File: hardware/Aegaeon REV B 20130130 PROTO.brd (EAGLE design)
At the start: 9.2 x 15.2 mm, 39 parts, among them IC1 ATTINY84A-MMH, Q1 DMN65D8LDW, U1 V_REG_LDOSMD

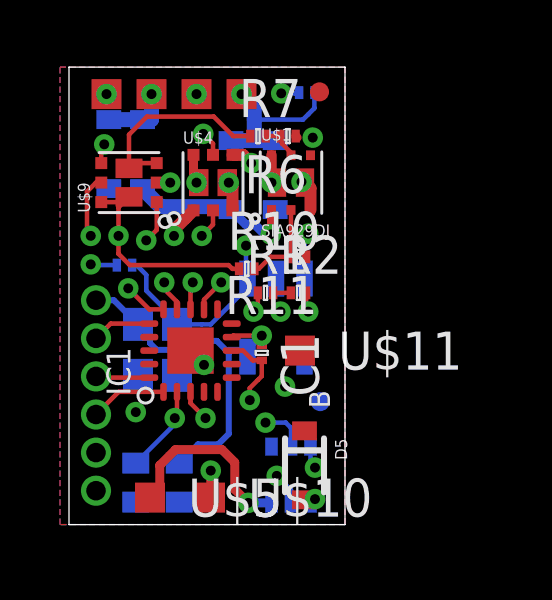
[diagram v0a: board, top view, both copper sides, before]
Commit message: Updated proto schematics to match new bridge design. Streamlined design in simulation file.
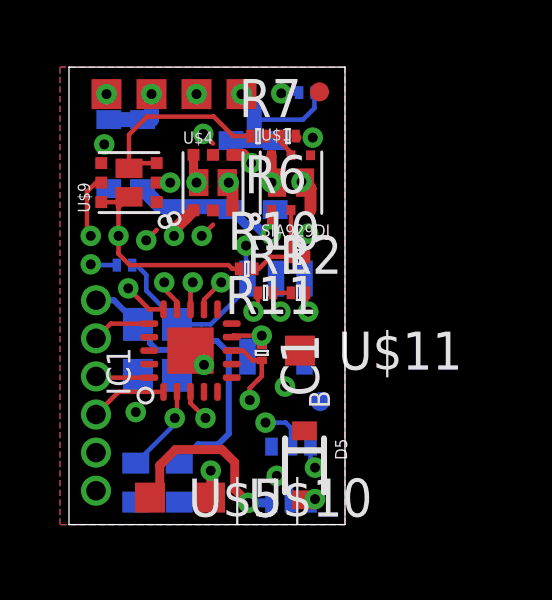
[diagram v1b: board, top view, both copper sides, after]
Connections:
- net FORWARD: now also U$4.G2, U$9.S2; no longer U$4.G1, U$9.G2
- net PWM: now also U$9.G1, U$9.G2; no longer U$9.S1, U$9.S2
- net REVERSE: now also U$4.G1, U$9.S1; no longer U$4.G2, U$9.G1
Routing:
- net PWM: track 8.59 -> 7.14 mm
- net REVERSE: track 9.67 -> 9.02 mm
- net FORWARD: track 11.0 -> 10.4 mm
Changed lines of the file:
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@@
 <?xml version="1.0" encoding="utf-8"?>
 <!DOCTYPE eagle SYSTEM "eagle.dtd">
-<eagle version="6.1">
+<eagle version="6.5.0">
 <drawing>
 <settings>
@@
 <text x="0" y="-4.5" size="1.016" layer="51">Copyright (C) 2012, Railstars Limited</text>
 <text x="0" y="-6" size="1.016" layer="51">All Rights Reserved</text>
-<dimension x1="0.3" y1="12.9" x2="9.5" y2="12.9" x3="4.9" y3="15.9" layer="51"/>
-<dimension x1="7.7" y1="0" x2="7.7" y2="15.25" x3="7.7" y3="7.625" layer="51" dtype="vertical"/>
+<dimension x1="0.3" y1="12.9" x2="9.5" y2="12.9" x3="4.9" y3="15.9" textsize="3.5" layer="51"/>
+<dimension x1="7.7" y1="0" x2="7.7" y2="15.25" x3="7.7" y3="7.625" textsize="3.5" layer="51" dtype="vertical"/>
 </plain>
 <attributes>
@@
 </class>
 </classes>
-<designrules>
+<designrules name="default">
 <description language="de">&lt;b&gt;EAGLE Design Rules&lt;/b&gt;
 &lt;p&gt;
@@
 </signal>
 <signal name="REVERSE">
-<contactref element="U$9" pad="G1"/>
-<contactref element="U$4" pad="G2"/>
 <via x="5.375" y="8.075" extent="1-16" drill="0.3302"/>
 <via x="3.675" y="11.4" extent="1-16" drill="0.3302"/>
 <via x="4.775" y="13.025" extent="1-16" drill="0.3302"/>
-<wire x1="3.225" y1="11.4" x2="3.5" y2="11.4" width="0.1524" layer="1"/>
 <wire x1="3.5" y1="11.4" x2="3.75" y2="11.65" width="0.1524" layer="1"/>
 <wire x1="3.75" y1="11.65" x2="3.75" y2="11.325" width="0.1524" layer="1"/>
@@
 <wire x1="4.1" y1="10.3" x2="3.675" y2="10.725" width="0.1524" layer="9"/>
 <wire x1="3.675" y1="11.4" x2="3.675" y2="10.725" width="0.1524" layer="9"/>
-<wire x1="5.1" y1="12.325" x2="5.1" y2="12.7" width="0.1524" layer="1"/>
 <wire x1="5.1" y1="12.7" x2="4.775" y2="13.025" width="0.1524" layer="1"/>
 <wire x1="5" y1="10.3" x2="5.3" y2="10" width="0.1524" layer="9"/>
@@
 <wire x1="4.8" y1="7.175" x2="4.8" y2="7.5" width="0.1524" layer="1"/>
 <wire x1="4.8" y1="7.5" x2="5.375" y2="8.075" width="0.1524" layer="1"/>
+<contactref element="U$9" pad="S1"/>
+<contactref element="U$4" pad="G1"/>
+<wire x1="5" y1="10.3" x2="5.1" y2="10.475" width="0" layer="19" extent="1-9"/>
+<wire x1="3.225" y1="10.75" x2="3.675" y2="10.725" width="0" layer="19" extent="1-9"/>
 </signal>
 <signal name="FORWARD">
-<contactref element="U$9" pad="G2"/>
-<contactref element="U$4" pad="G1"/>
 <contactref element="IC1" pad="P$15"/>
 <via x="1.025" y="9.625" extent="1-16" drill="0.3302"/>
@@
 <wire x1="2.275" y1="7.875" x2="2.175" y2="7.975" width="0.1524" layer="9"/>
 <wire x1="1.025" y1="9.625" x2="2.175" y2="8.475" width="0.1524" layer="9"/>
-<wire x1="1.375" y1="11.4" x2="1.2" y2="11.4" width="0.1524" layer="1"/>
 <wire x1="1.2" y1="11.4" x2="0.9" y2="11.1" width="0.1524" layer="1"/>
 <wire x1="1.025" y1="9.625" x2="0.9" y2="9.75" width="0.1524" layer="1"/>
@@
 <wire x1="3.45" y1="7.175" x2="2.975" y2="7.175" width="0.1524" layer="1"/>
 <wire x1="2.975" y1="7.175" x2="2.275" y2="7.875" width="0.1524" layer="1"/>
-<wire x1="5.1" y1="10.475" x2="5.1" y2="10" width="0.1524" layer="1"/>
 <wire x1="5.1" y1="10" x2="4.725" y2="9.625" width="0.1524" layer="1"/>
 <wire x1="4.725" y1="9.625" x2="4.15" y2="10.2" width="0.1524" layer="8"/>
@@
 <wire x1="1.025" y1="9.625" x2="1.6" y2="10.2" width="0.1524" layer="8"/>
 <wire x1="1.6" y1="10.2" x2="1.775" y2="10.2" width="0.1524" layer="8"/>
+<contactref element="U$9" pad="S2"/>
+<contactref element="U$4" pad="G2"/>
+<wire x1="5.1" y1="10" x2="5.1" y2="12.325" width="0" layer="19" extent="1-1"/>
+<wire x1="1.375" y1="12.05" x2="1.2" y2="11.4" width="0" layer="19" extent="1-1"/>
 </signal>
 <signal name="BEMF">
@@
 </signal>
 <signal name="PWM">
-<contactref element="U$9" pad="S2"/>
-<contactref element="U$9" pad="S1"/>
 <via x="2.875" y="9.475" extent="1-16" drill="0.3302"/>
 <via x="1.475" y="12.675" extent="1-16" drill="0.3302"/>
-<wire x1="1.375" y1="12.05" x2="1.375" y2="12.575" width="0.1524" layer="1"/>
-<wire x1="3.225" y1="10.75" x2="3.225" y2="9.825" width="0.1524" layer="1"/>
 <wire x1="3.225" y1="9.825" x2="2.875" y2="9.475" width="0.1524" layer="1"/>
 <contactref element="IC1" pad="P$14"/>
@@
 <wire x1="1.75" y1="11.05" x2="1.75" y2="12.4" width="0.1524" layer="9"/>
 <wire x1="1.75" y1="12.4" x2="1.475" y2="12.675" width="0.1524" layer="9"/>
+<contactref element="U$9" pad="G2"/>
+<contactref element="U$9" pad="G1"/>
+<wire x1="1.75" y1="11.05" x2="3.225" y2="11.4" width="0" layer="19" extent="1-9"/>
+<wire x1="1.375" y1="11.4" x2="1.75" y2="11.05" width="0" layer="19" extent="1-9"/>
 </signal>
 </signals>

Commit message: Saved files.
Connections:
- net FORWARD: now also U$4.G1, U$9.S1; no longer U$4.G2, U$9.S2
- net REVERSE: now also U$4.G2, U$9.S2; no longer U$4.G1, U$9.S1
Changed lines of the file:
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@@
 <layer number="6" name="Route6" color="1" fill="8" visible="no" active="no"/>
 <layer number="7" name="Route7" color="4" fill="8" visible="no" active="no"/>
-<layer number="8" name="Route8" color="5" fill="1" visible="no" active="yes"/>
+<layer number="8" name="Route8" color="5" fill="1" visible="yes" active="yes"/>
 <layer number="9" name="Route9" color="3" fill="1" visible="yes" active="yes"/>
 <layer number="10" name="Route10" color="1" fill="7" visible="no" active="no"/>
@@
 <wire x1="4.8" y1="7.175" x2="4.8" y2="7.5" width="0.1524" layer="1"/>
 <wire x1="4.8" y1="7.5" x2="5.375" y2="8.075" width="0.1524" layer="1"/>
-<contactref element="U$9" pad="S1"/>
-<contactref element="U$4" pad="G1"/>
-<wire x1="5" y1="10.3" x2="5.1" y2="10.475" width="0" layer="19" extent="1-9"/>
-<wire x1="3.225" y1="10.75" x2="3.675" y2="10.725" width="0" layer="19" extent="1-9"/>
+<contactref element="U$9" pad="S2"/>
+<contactref element="U$4" pad="G2"/>
+<wire x1="5.1" y1="12.7" x2="5.1" y2="12.325" width="0" layer="19" extent="1-1"/>
+<wire x1="1.375" y1="12.05" x2="3.5" y2="11.4" width="0" layer="19" extent="1-1"/>
 </signal>
 <signal name="FORWARD">
@@
 <wire x1="1.025" y1="9.625" x2="1.6" y2="10.2" width="0.1524" layer="8"/>
 <wire x1="1.6" y1="10.2" x2="1.775" y2="10.2" width="0.1524" layer="8"/>
-<contactref element="U$9" pad="S2"/>
-<contactref element="U$4" pad="G2"/>
-<wire x1="5.1" y1="10" x2="5.1" y2="12.325" width="0" layer="19" extent="1-1"/>
-<wire x1="1.375" y1="12.05" x2="1.2" y2="11.4" width="0" layer="19" extent="1-1"/>
+<contactref element="U$9" pad="S1"/>
+<contactref element="U$4" pad="G1"/>
+<wire x1="5.1" y1="10" x2="5.1" y2="10.475" width="0" layer="19" extent="1-1"/>
+<wire x1="3.225" y1="10.75" x2="4.15" y2="10.2" width="0" layer="19" extent="1-8"/>
 </signal>
 <signal name="BEMF">
